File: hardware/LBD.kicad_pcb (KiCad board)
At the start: 2 copper layers, 13.4 x 46.9 mm, 10 parts, among them J2 USB4155-03-C_REVA, U1 RP2040, U4 TPSM828214SILR

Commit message: feat: place components
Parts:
- added C10: 100n, Capacitor_SMD:C_0201_0603Metric, F.Cu at (166.1, 92.4)
- added C11: 100n, Capacitor_SMD:C_0201_0603Metric, F.Cu at (166.1, 94.1)
- added C12: 100n, Capacitor_SMD:C_0201_0603Metric, F.Cu at (166.1, 95.9)
- added C13: 100n, Capacitor_SMD:C_0201_0603Metric, F.Cu at (166.1, 97.6)
- added C14: 4.7u, Capacitor_SMD:C_0603_1608Metric, F.Cu at (171.8, 92.8)
- added C15: 22u, Capacitor_SMD:C_0603_1608Metric, F.Cu at (171.8, 95.3)
- added C16: 100n, Capacitor_SMD:C_0201_0603Metric, F.Cu at (163.6, 105.6)
- added C17: 100n, Capacitor_SMD:C_0201_0603Metric, F.Cu at (168.5, 92.4)
- added C18: 100n, Capacitor_SMD:C_0201_0603Metric, F.Cu at (168.5, 94.1)
- added C19: 1u, Capacitor_SMD:C_0402_1005Metric, F.Cu at (167.9, 99.5)
- added C20: 1u, Capacitor_SMD:C_0402_1005Metric, F.Cu at (167.9, 101.5)
- added C21: 10u, Capacitor_SMD:C_0603_1608Metric, F.Cu at (143.6, 92.8)
- added C4: 15p, Capacitor_SMD:C_0201_0603Metric, F.Cu at (157.6, 101.7)
- added C5: 15p, Capacitor_SMD:C_0201_0603Metric, F.Cu at (157.6, 103.4)
- added C6: 100n, Capacitor_SMD:C_0201_0603Metric, F.Cu at (163.6, 92.4)
- added C7: 100n, Capacitor_SMD:C_0201_0603Metric, F.Cu at (163.6, 94.1)
- added C8: 100n, Capacitor_SMD:C_0201_0603Metric, F.Cu at (163.6, 95.9)
- added C9: 100n, Capacitor_SMD:C_0201_0603Metric, F.Cu at (163.6, 97.6)
- added D8: IN-S126ESGHIR, LBD_Footprints:LED_IN-S12_INL, F.Cu at (138.8, 125.9)
- added J1: Conn_01x03_Pin, Connector_PinHeader_2.54mm:PinHeader_1x03_P2.54mm_Vertical_SMD_Pin1Left, F.Cu at (152.5, 105.6)
- added Q1: AO3400A, Package_TO_SOT_SMD:SOT-23, F.Cu at (144.1, 108.8)
- added R10: 100k, Resistor_SMD:R_0201_0603Metric, F.Cu at (168.5, 95.9)
- added R11: 22, Resistor_SMD:R_0201_0603Metric, F.Cu at (161.9, 115.1)
- added R12: 22, Resistor_SMD:R_0201_0603Metric, F.Cu at (161.9, 116.9)
- added R13: 5.1k, Resistor_SMD:R_0201_0603Metric, F.Cu at (161.9, 118.6)
- added R14: 22, Resistor_SMD:R_0603_1608Metric, F.Cu at (143.6, 95.3)
- added R15: 22, Resistor_SMD:R_0603_1608Metric, F.Cu at (143.6, 97.8)
- added R16: 22, Resistor_SMD:R_0603_1608Metric, F.Cu at (143.6, 100.3)
- added R17: 22, Resistor_SMD:R_0603_1608Metric, F.Cu at (143.6, 102.8)
- added R18: 10k, Resistor_SMD:R_0201_0603Metric, F.Cu at (142.8, 111.9)
- added R19: 33, Resistor_SMD:R_0603_1608Metric, F.Cu at (143.6, 105.3)
- added R3: 5.1k, Resistor_SMD:R_0201_0603Metric, F.Cu at (161.9, 113.4)
- added R6: 1k (0603), Resistor_SMD:R_0603_1608Metric, F.Cu at (158.4, 107.3)
- added R7: 1k, Resistor_SMD:R_0201_0603Metric, F.Cu at (163.6, 107.3)
- added R8: 10k, Resistor_SMD:R_0201_0603Metric, F.Cu at (163.6, 109.1)
- added R9: 10k, Resistor_SMD:R_0201_0603Metric, F.Cu at (157.6, 105.2)
- added SW2: BOOTSEL, Button_Switch_SMD:SW_SPST_B3U-1000P, F.Cu at (167.8, 106.9)
- D1, D2, D3, D4, D5, D6, D7: value LED -> IN-S126ESGHIR
- J2: value USB4155-03-C_REVA -> USB4155-03-C
- moved D7 41.4 mm to (138.8, 121.4)
- moved D5 31.4 mm to (138.8, 112.4), turned to 0 degrees
- moved U1 20.0 mm to (153.6, 96.2)
- moved U4 15.4 mm to (164.8, 100.6)
- moved D6 15.2 mm to (138.8, 116.9), turned to 0 degrees
- moved J2 11.5 mm to (154.6, 115.3)
- moved D1 8.93 mm to (138.8, 94.4), turned to 0 degrees
- moved D2 8.28 mm to (138.8, 98.9), turned to 0 degrees
- moved D3 7.65 mm to (138.8, 103.4), turned to 0 degrees
- moved D4 4.42 mm to (138.8, 107.9), turned to 0 degrees
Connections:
- D1 pad 1: unconnected-(D1-K-Pad1) -> Net-(D1-K)
- D1 pad 2: unconnected-(D1-A-Pad2) -> Net-(D1-A)
- D2 pad 1: unconnected-(D2-K-Pad1) -> Net-(D2-K)
- D2 pad 2: unconnected-(D2-A-Pad2) -> Net-(D2-A)
- D3 pad 1: unconnected-(D3-K-Pad1) -> Net-(D3-K)
- D3 pad 2: unconnected-(D3-A-Pad2) -> Net-(D3-A)
- D4 pad 1: unconnected-(D4-K-Pad1) -> Net-(D4-K)
- D4 pad 2: unconnected-(D4-A-Pad2) -> Net-(D4-A)
- D5 pad 1: unconnected-(D5-K-Pad1) -> Net-(D5-K)
- D5 pad 2: unconnected-(D5-A-Pad2) -> Net-(D1-K)
- D6 pad 1: unconnected-(D6-K-Pad1) -> Net-(D5-K)
- D6 pad 2: unconnected-(D6-A-Pad2) -> Net-(D2-K)
- D7 pad 1: unconnected-(D7-K-Pad1) -> Net-(D5-K)
- D7 pad 2: unconnected-(D7-A-Pad2) -> Net-(D3-K)
- U1 pad 4: unconnected-(U1-GPIO2-Pad4) -> /Infared/IR_GATE
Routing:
- net GND: track 41.4 -> 0.00 mm
- net +3.3V: track 32.2 -> 0.00 mm, vias 2 -> 0
- net VBUS: track 26.7 -> 0.00 mm
- net +1V1: track 14.5 -> 0.00 mm, vias 2 -> 0
- net /Power/PG: track 13.4 -> 0.00 mm, vias 2 -> 0
- net /USB/DN: track 1.69 -> 0.00 mm
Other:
- board outline removed

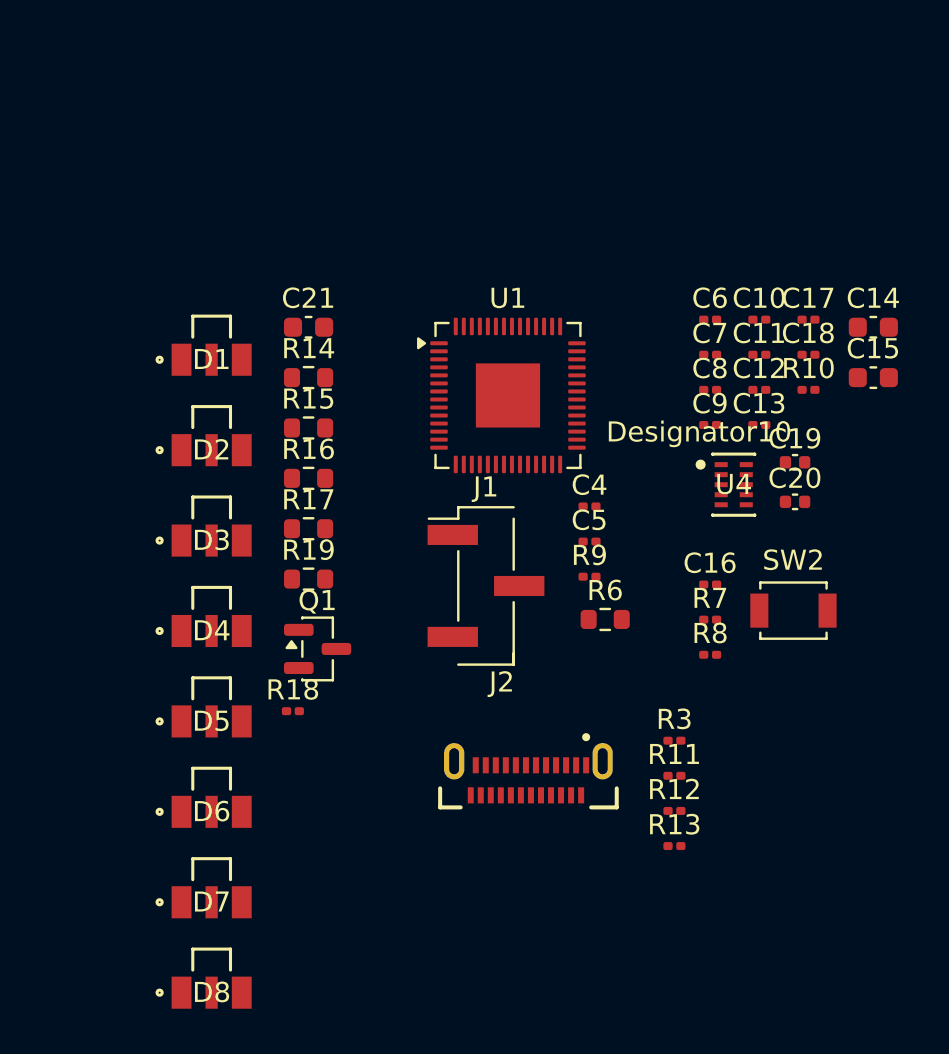
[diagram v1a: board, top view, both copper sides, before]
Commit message: feat: place pcb components
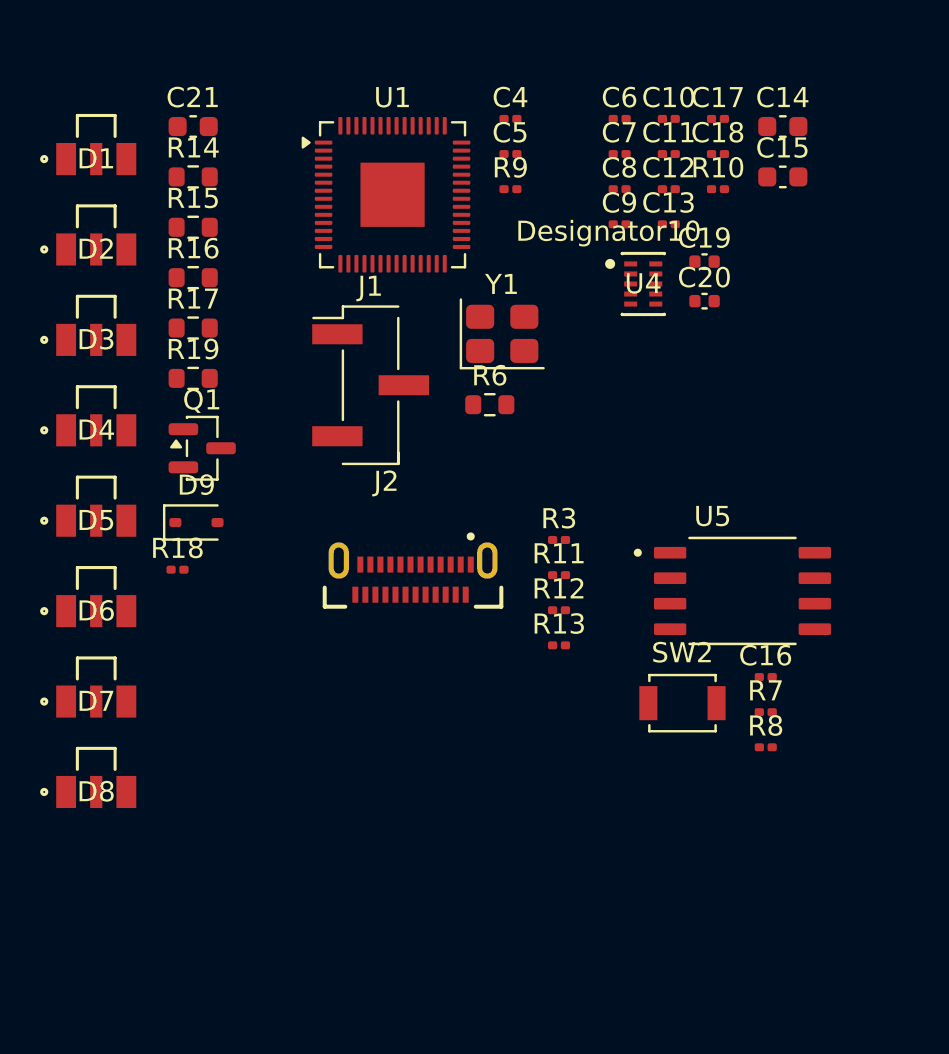
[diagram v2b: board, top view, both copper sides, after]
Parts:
- added D9: MM3Z6V2, Diode_SMD:D_SOD-323, F.Cu at (138.0, 102.5)
- added U5: W25Q128JVSIQ, LBD_Footprints:W25Q128JVSIQ, F.Cu at (165.2, 105.9)
- added Y1: 12 MHz, Crystal:Crystal_SMD_3225-4Pin_3.2x2.5mm, F.Cu at (153.3, 93.1)
- moved C4 19.7 mm to (153.7, 82.4)
- moved C5 19.7 mm to (153.7, 84.1)
- moved R9 19.7 mm to (153.7, 85.9)
- moved R6 12.1 mm to (152.7, 96.6)
- moved C21 11.5 mm to (137.9, 82.8)
- moved D1 11.5 mm to (133.0, 84.4)
- moved D2 11.5 mm to (133.0, 88.9)
- moved D3 11.5 mm to (133.0, 93.4)
- moved D4 11.5 mm to (133.0, 97.9)
- moved D5 11.5 mm to (133.0, 102.4)
- moved D6 11.5 mm to (133.0, 106.9)
- moved D7 11.5 mm to (133.0, 111.4)
- moved D8 11.5 mm to (133.0, 115.9)
- moved J1 11.5 mm to (146.7, 95.6)
- moved J2 11.5 mm to (148.8, 105.3)
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
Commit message: feat: make board 4 layers
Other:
- copper layers 2 -> 4
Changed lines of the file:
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@@
 	(layers
 		(0 "F.Cu" signal)
+		(4 "In1.Cu" signal)
+		(6 "In2.Cu" signal)
 		(2 "B.Cu" signal)
 		(9 "F.Adhes" user "F.Adhesive")
@@
 	)
 	(setup
+		(stackup
+			(layer "F.SilkS"
+				(type "Top Silk Screen")
+			)
+			(layer "F.Paste"
+				(type "Top Solder Paste")
+			)
+			(layer "F.Mask"
+				(type "Top Solder Mask")
+				(thickness 0.01)
+			)
+			(layer "F.Cu"
+				(type "copper")
+				(thickness 0.035)
+			)
+			(layer "dielectric 1"
+				(type "prepreg")
+				(thickness 0.1)
+				(material "FR4")
+				(epsilon_r 4.5)
+				(loss_tangent 0.02)
+			)
+			(layer "In1.Cu"
+				(type "copper")
+				(thickness 0.035)
+			)
+			(layer "dielectric 2"
+				(type "core")
+				(thickness 1.24)
+				(material "FR4")
+				(epsilon_r 4.5)
+				(loss_tangent 0.02)
+			)
+			(layer "In2.Cu"
+				(type "copper")
+				(thickness 0.035)
+			)
+			(layer "dielectric 3"
+				(type "prepreg")
+				(thickness 0.1)
+				(material "FR4")
+				(epsilon_r 4.5)
+				(loss_tangent 0.02)
+			)
+			(layer "B.Cu"
+				(type "copper")
+				(thickness 0.035)
+			)
+			(layer "B.Mask"
+				(type "Bottom Solder Mask")
+				(thickness 0.01)
+			)
+			(layer "B.Paste"
+				(type "Bottom Solder Paste")
+			)
+			(layer "B.SilkS"
+				(type "Bottom Silk Screen")
+			)
+			(copper_finish "None")
+			(dielectric_constraints no)
+		)
 		(pad_to_mask_clearance 0)
 		(allow_soldermask_bridges_in_footprints no)
@@
 		(capping no)
 		(filling no)
+		(zone_defaults)
 		(pcbplotparams
 			(layerselection 0x00000000_00000000_55555555_5755f5ff)
